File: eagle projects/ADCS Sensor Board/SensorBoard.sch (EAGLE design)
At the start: 85 parts, among them J5 HDR_10_EZFET_DEBUGGER, J6 MTI-1_8428-11B1-RK-TP, Q1 BC850SMD, Q2 IRF7507TRPBF, U1 MSP430F5529IPN, U2 LMV321, U3 ADS7841E_2K5, U4 LMV321, U5 LM20BIM7X_NOPB, U6 LMV321, Y1 32.768kHz, Y2 CSTCR4M00G15L99

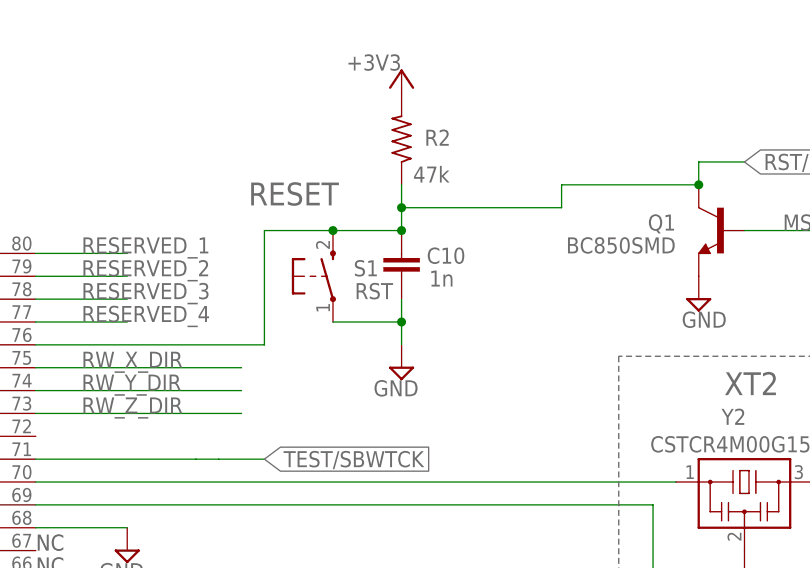
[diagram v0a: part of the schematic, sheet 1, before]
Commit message: Added copper pours to top and bottom. Fixed silksreens, smoothed traces
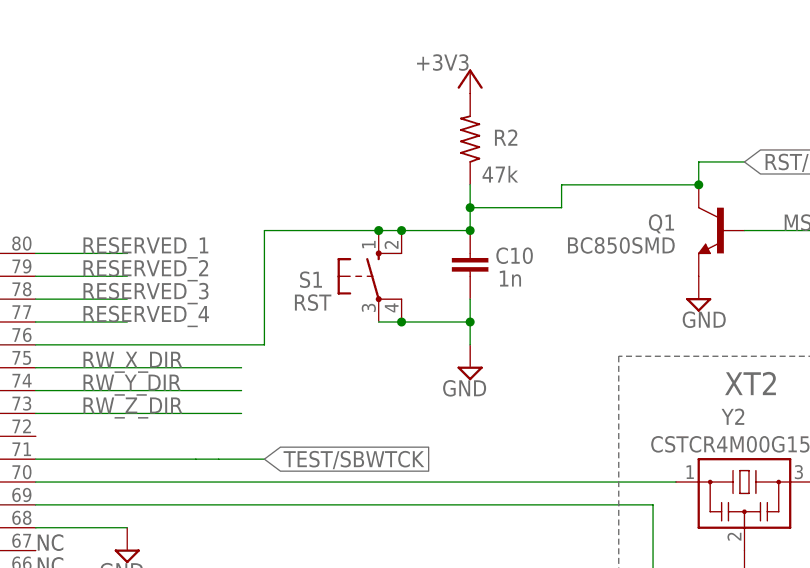
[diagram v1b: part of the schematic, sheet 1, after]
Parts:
- removed SJ1: (no value), jumper:SJ
- added R100: 0R, rcl:R-US_R0603
- JP1: device jumper:JP1Q -> my_library:JP1Q_
- JP2, JP3: device pinhead:PINHD-2X8 -> my_library:PINHD-2X8
- JP4: device pinhead:PINHD-2X6 -> my_library:PINHD-2X6
- JP7: device pinhead:PINHD-1X7 -> my_library:PINHD-1X7
- S1: device electricalmeter:PB -> my_library:10-XX
- TP6: value TPPAD1-13 -> TPB1,27; device testpad:TPPAD1-13 -> testpad:TPB1,27
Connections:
- net GND: now also S1.P1
- net N$35: now also R100.1; no longer SJ1.1
- net N$37: now also R100.2; no longer SJ1.2
- net RST/SBWTDIO: now also S1.S1
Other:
- note removed: "RESET"
- moved on the sheet: C10, R2

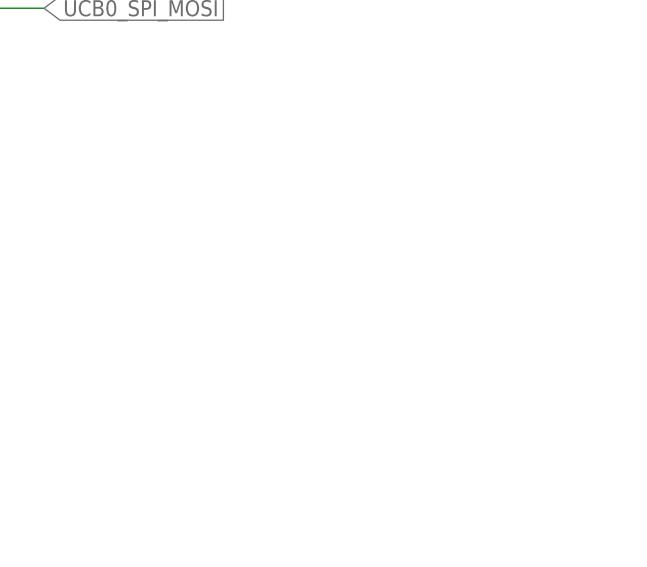
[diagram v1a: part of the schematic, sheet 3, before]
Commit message: Added spi bus test headers
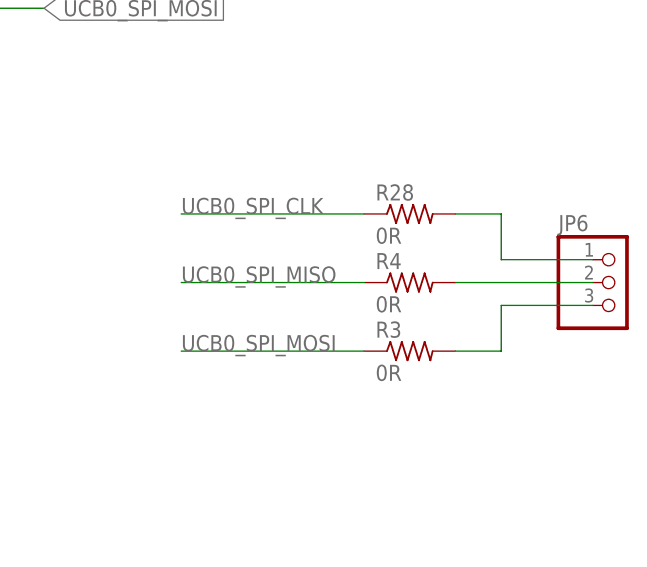
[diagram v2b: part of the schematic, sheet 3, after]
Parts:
- added JP6: (no value), my_library:PINHD-1X3
- added R28, R3, R4: 0R, rcl:R-US_R0805
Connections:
- new net N$1: JP6.1, R28.2
- new net N$2: JP6.2, R4.2
- new net N$3: JP6.3, R3.2
- net UCB0_SPI_CLK: now also R28.1
- net UCB0_SPI_MISO: now also R4.1
- net UCB0_SPI_MOSI: now also R3.1
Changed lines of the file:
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@@
 <schematic_group name="POWER_CONNECTOR"/>
 <schematic_group name="PAYLOAD_CAMERAS"/>
+<schematic_group name="SPI_BUS_TEST"/>
 </groups>
 <parts>
@@
 <part name="SUPPLY31" library="supply2" library_urn="urn:adsk.eagle:library:372" deviceset="GND" device=""/>
 <part name="SUPPLY32" library="supply2" library_urn="urn:adsk.eagle:library:372" deviceset="GND" device=""/>
-<part name="U1" library="my_library" library_urn="urn:adsk.eagle:library:22876504" deviceset="MSP430F5529IPN" device="" package3d_urn="urn:adsk.eagle:package:22927473/4"/>
+<part name="U1" library="my_library" library_urn="urn:adsk.eagle:library:22876504" deviceset="MSP430F5529IPN" device="" package3d_urn="urn:adsk.eagle:package:22927473/5"/>
 <part name="SUPPLY1" library="supply2" library_urn="urn:adsk.eagle:library:372" deviceset="GND" device=""/>
 <part name="SUPPLY2" library="supply2" library_urn="urn:adsk.eagle:library:372" deviceset="GND" device=""/>
@@
 <part name="+3V3" library="supply1" library_urn="urn:adsk.eagle:library:371" deviceset="+3V3" device=""/>
 <part name="S1" library="my_library" library_urn="urn:adsk.eagle:library:22876504" deviceset="10-XX" device="" package3d_urn="urn:adsk.eagle:package:24526167/2" value="RST"/>
+<part name="JP6" library="my_library" library_urn="urn:adsk.eagle:library:22876504" deviceset="PINHD-1X3" device="" package3d_urn="urn:adsk.eagle:package:24583855/1"/>
+<part name="R3" library="rcl" library_urn="urn:adsk.eagle:library:334" deviceset="R-US_" device="R0805" package3d_urn="urn:adsk.eagle:package:23553/2" value="0R"/>
+<part name="R4" library="rcl" library_urn="urn:adsk.eagle:library:334" deviceset="R-US_" device="R0805" package3d_urn="urn:adsk.eagle:package:23553/2" value="0R"/>
+<part name="R28" library="rcl" library_urn="urn:adsk.eagle:library:334" deviceset="R-US_" device="R0805" package3d_urn="urn:adsk.eagle:package:23553/2" value="0R"/>
 </parts>
 <sheets>
@@
 <attribute name="VALUE" x="88.9" y="63.5" size="1.778" layer="96" rot="R180"/>
 </instance>
+<instance part="JP6" gate="A" x="254" y="99.06" smashed="yes" grouprefs="SPI_BUS_TEST">
+<attribute name="NAME" x="247.65" y="104.775" size="1.778" layer="95"/>
+<attribute name="VALUE" x="247.65" y="91.44" size="1.778" layer="96"/>
+</instance>
+<instance part="R3" gate="G$1" x="231.14" y="91.44" smashed="yes" grouprefs="SPI_BUS_TEST">
+<attribute name="NAME" x="227.33" y="92.9386" size="1.778" layer="95"/>
+<attribute name="VALUE" x="227.33" y="88.138" size="1.778" layer="96"/>
+</instance>
+<instance part="R4" gate="G$1" x="231.14" y="99.06" smashed="yes" grouprefs="SPI_BUS_TEST">
+<attribute name="NAME" x="227.33" y="100.5586" size="1.778" layer="95"/>
+<attribute name="VALUE" x="227.33" y="95.758" size="1.778" layer="96"/>
+</instance>
+<instance part="R28" gate="G$1" x="231.14" y="106.68" smashed="yes" grouprefs="SPI_BUS_TEST">
+<attribute name="NAME" x="227.33" y="108.1786" size="1.778" layer="95"/>
+<attribute name="VALUE" x="227.33" y="103.378" size="1.778" layer="96"/>
+</instance>
 </instances>
 <busses>
@@
 <label x="190.5" y="134.62" size="1.778" layer="95" xref="yes"/>
 </segment>
+<segment>
+<pinref part="R28" gate="G$1" pin="1"/>
+<wire x1="226.06" y1="106.68" x2="205.74" y2="106.68" width="0.1524" layer="91" grouprefs="SPI_BUS_TEST"/>
+<label x="205.74" y="106.68" size="1.778" layer="95" grouprefs="SPI_BUS_TEST"/>
+</segment>
 </net>
 <net name="UCB0_SPI_MOSI" class="0">
@@
 <label x="190.5" y="129.54" size="1.778" layer="95" xref="yes"/>
 </segment>
+<segment>
+<pinref part="R3" gate="G$1" pin="1"/>
+<wire x1="205.74" y1="91.44" x2="226.06" y2="91.44" width="0.1524" layer="91" grouprefs="SPI_BUS_TEST"/>
+<label x="205.74" y="91.44" size="1.778" layer="95" grouprefs="SPI_BUS_TEST"/>
+</segment>
 </net>
 <net name="UCB0_SPI_MISO" class="0">
@@
 <wire x1="160.02" y1="132.08" x2="167.64" y2="132.08" width="0.1524" layer="91"/>
 <label x="167.64" y="132.08" size="1.778" layer="95" xref="yes"/>
+</segment>
+<segment>
+<pinref part="R4" gate="G$1" pin="1"/>
+<wire x1="205.74" y1="99.06" x2="226.06" y2="99.06" width="0.1524" layer="91" grouprefs="SPI_BUS_TEST"/>
+<label x="205.74" y="99.06" size="1.778" layer="95" grouprefs="SPI_BUS_TEST"/>
 </segment>
 </net>
@@
 </segment>
 </net>
+<net name="N$1" class="0">
+<segment>
+<pinref part="R28" gate="G$1" pin="2"/>
+<pinref part="JP6" gate="A" pin="1"/>
+<wire x1="236.22" y1="106.68" x2="241.3" y2="106.68" width="0.1524" layer="91" grouprefs="SPI_BUS_TEST"/>
+<wire x1="241.3" y1="106.68" x2="241.3" y2="101.6" width="0.1524" layer="91" grouprefs="SPI_BUS_TEST"/>
+<wire x1="241.3" y1="101.6" x2="251.46" y2="101.6" width="0.1524" layer="91" grouprefs="SPI_BUS_TEST"/>
+</segment>
+</net>
+<net name="N$2" class="0">
+<segment>
+<pinref part="R4" gate="G$1" pin="2"/>
+<pinref part="JP6" gate="A" pin="2"/>
+<wire x1="236.22" y1="99.06" x2="251.46" y2="99.06" width="0.1524" layer="91" grouprefs="SPI_BUS_TEST"/>
+</segment>
+</net>
+<net name="N$3" class="0">
+<segment>
+<pinref part="R3" gate="G$1" pin="2"/>
+<pinref part="JP6" gate="A" pin="3"/>
+<wire x1="251.46" y1="96.52" x2="241.3" y2="96.52" width="0.1524" layer="91" grouprefs="SPI_BUS_TEST"/>
+<wire x1="241.3" y1="96.52" x2="241.3" y2="91.44" width="0.1524" layer="91" grouprefs="SPI_BUS_TEST"/>
+<wire x1="241.3" y1="91.44" x2="236.22" y2="91.44" width="0.1524" layer="91" grouprefs="SPI_BUS_TEST"/>
+</segment>
+</net>

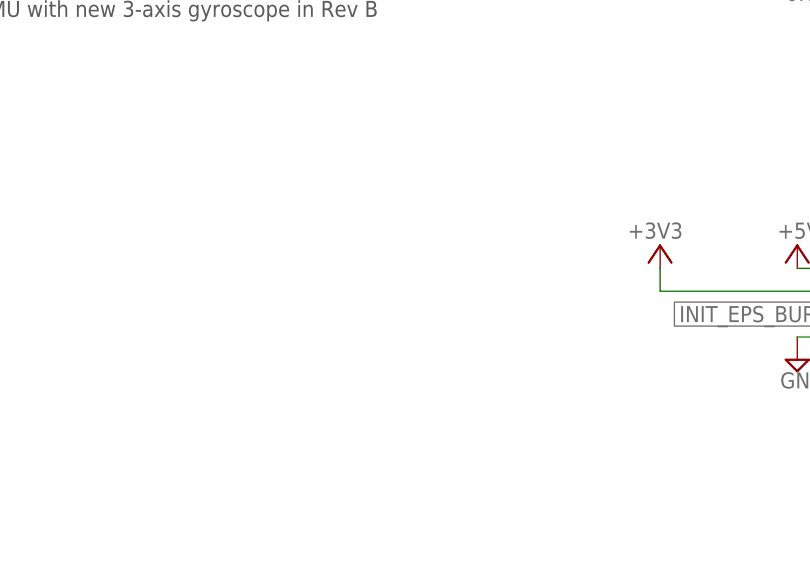
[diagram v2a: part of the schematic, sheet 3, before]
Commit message: added indicator LEDs, drill legend, and adjusted board thickness
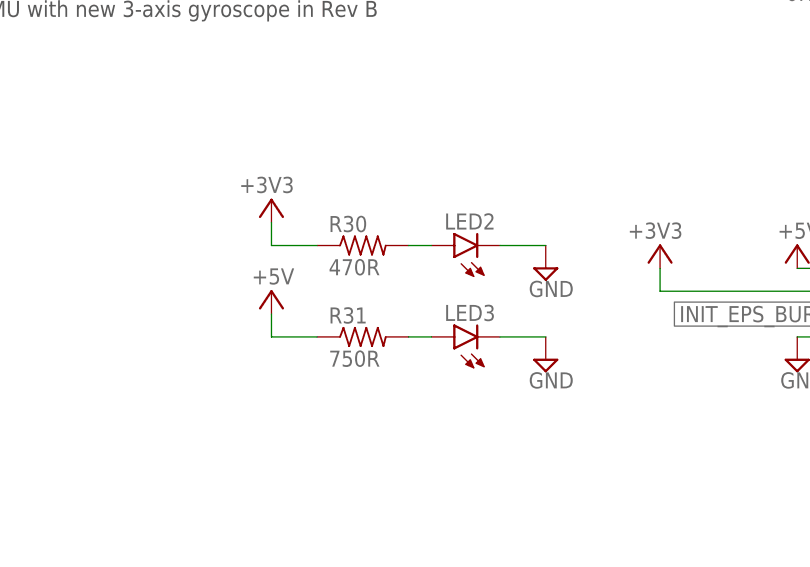
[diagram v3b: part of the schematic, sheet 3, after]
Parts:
- added LED1, LED2, LED3: (no value), led:LEDCHIP-LED0603
- added R29, R30: 470R, rcl:R-US_R0603
- added R31: 750R, rcl:R-US_R0603
- R100: device rcl:R-US_R0603 -> rcl:R-US_R0805
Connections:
- new net N$4: LED1.A, R29.2
- new net N$5: LED2.A, R30.2
- new net N$6: LED3.A, R31.2
- net +3V3: now also R30.1
- net +5V: now also R31.1
- net GND: now also LED1.C, LED2.C, LED3.C
- net MSP430_ACTIVE: now also R29.1
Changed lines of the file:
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@@
 <part name="MH3" library="my_library" library_urn="urn:adsk.eagle:library:22876504" deviceset="MTGP700H400" device="" package3d_urn="urn:adsk.eagle:package:23248012/2"/>
 <part name="MH4" library="my_library" library_urn="urn:adsk.eagle:library:22876504" deviceset="MTGP700H400" device="" package3d_urn="urn:adsk.eagle:package:23248012/2"/>
-<part name="R100" library="rcl" library_urn="urn:adsk.eagle:library:334" deviceset="R-US_" device="R0603" package3d_urn="urn:adsk.eagle:package:23555/3" value="0R"/>
+<part name="R100" library="rcl" library_urn="urn:adsk.eagle:library:334" deviceset="R-US_" device="R0805" package3d_urn="urn:adsk.eagle:package:23553/2" value="0R"/>
 <part name="C20" library="rcl" library_urn="urn:adsk.eagle:library:334" deviceset="C-EU" device="C0805" package3d_urn="urn:adsk.eagle:package:23617/2" value="1n"/>
 <part name="C19" library="rcl" library_urn="urn:adsk.eagle:library:334" deviceset="C-EU" device="C0603" package3d_urn="urn:adsk.eagle:package:23616/2" value="0.1u"/>
@@
 <part name="R4" library="rcl" library_urn="urn:adsk.eagle:library:334" deviceset="R-US_" device="R0805" package3d_urn="urn:adsk.eagle:package:23553/2" value="0R"/>
 <part name="R28" library="rcl" library_urn="urn:adsk.eagle:library:334" deviceset="R-US_" device="R0805" package3d_urn="urn:adsk.eagle:package:23553/2" value="0R"/>
+<part name="SUPPLY13" library="supply2" library_urn="urn:adsk.eagle:library:372" deviceset="GND" device=""/>
+<part name="R29" library="rcl" library_urn="urn:adsk.eagle:library:334" deviceset="R-US_" device="R0603" package3d_urn="urn:adsk.eagle:package:23555/3" value="470R"/>
+<part name="LED1" library="led" library_urn="urn:adsk.eagle:library:259" deviceset="LED" device="CHIP-LED0603" package3d_urn="urn:adsk.eagle:package:15819/3"/>
+<part name="LED2" library="led" library_urn="urn:adsk.eagle:library:259" deviceset="LED" device="CHIP-LED0603" package3d_urn="urn:adsk.eagle:package:15819/3"/>
+<part name="LED3" library="led" library_urn="urn:adsk.eagle:library:259" deviceset="LED" device="CHIP-LED0603" package3d_urn="urn:adsk.eagle:package:15819/3"/>
+<part name="R30" library="rcl" library_urn="urn:adsk.eagle:library:334" deviceset="R-US_" device="R0603" package3d_urn="urn:adsk.eagle:package:23555/3" value="470R"/>
+<part name="R31" library="rcl" library_urn="urn:adsk.eagle:library:334" deviceset="R-US_" device="R0603" package3d_urn="urn:adsk.eagle:package:23555/3" value="750R"/>
+<part name="SUPPLY19" library="supply2" library_urn="urn:adsk.eagle:library:372" deviceset="GND" device=""/>
+<part name="SUPPLY25" library="supply2" library_urn="urn:adsk.eagle:library:372" deviceset="GND" device=""/>
+<part name="+3V4" library="supply1" library_urn="urn:adsk.eagle:library:371" deviceset="+3V3" device=""/>
+<part name="P+2" library="supply1" library_urn="urn:adsk.eagle:library:371" deviceset="+5V" device=""/>
 </parts>
 <sheets>
@@
 <attribute name="VALUE" x="201.295" y="166.37" size="1.778" layer="96"/>
 </instance>
+<instance part="SUPPLY13" gate="GND" x="266.7" y="40.64" smashed="yes">
+<attribute name="VALUE" x="264.795" y="37.465" size="1.778" layer="96"/>
+</instance>
+<instance part="R29" gate="G$1" x="246.38" y="43.18" smashed="yes">
+<attribute name="NAME" x="242.57" y="44.6786" size="1.778" layer="95"/>
+<attribute name="VALUE" x="242.57" y="39.878" size="1.778" layer="96"/>
+</instance>
+<instance part="LED1" gate="G$1" x="256.54" y="43.18" smashed="yes" rot="R90">
+<attribute name="NAME" x="261.112" y="46.736" size="1.778" layer="95" rot="R180"/>
+<attribute name="VALUE" x="261.112" y="48.895" size="1.778" layer="96" rot="R180"/>
+</instance>
 </instances>
 <busses>
@@
 <wire x1="172.72" y1="134.62" x2="210.82" y2="134.62" width="0.1524" layer="91"/>
 <pinref part="SUPPLY11" gate="GND" pin="GND"/>
+</segment>
+<segment>
+<pinref part="LED1" gate="G$1" pin="C"/>
+<pinref part="SUPPLY13" gate="GND" pin="GND"/>
+<wire x1="261.62" y1="43.18" x2="266.7" y2="43.18" width="0.1524" layer="91"/>
 </segment>
 </net>
@@
 <wire x1="213.36" y1="43.18" x2="241.3" y2="43.18" width="0.1524" layer="91"/>
 <label x="220.98" y="43.18" size="1.778" layer="95"/>
+<pinref part="R29" gate="G$1" pin="1"/>
 </segment>
 <segment>
@@
 <pinref part="JP2" gate="A" pin="13"/>
 <label x="22.86" y="40.64" size="1.778" layer="95" grouprefs="ACTUATOR_BOARD_CONNECTORS"/>
+</segment>
+</net>
+<net name="N$4" class="0">
+<segment>
+<pinref part="LED1" gate="G$1" pin="A"/>
+<pinref part="R29" gate="G$1" pin="2"/>
+<wire x1="254" y1="43.18" x2="251.46" y2="43.18" width="0.1524" layer="91"/>
 </segment>
 </net>
@@
 <attribute name="VALUE" x="227.33" y="103.378" size="1.778" layer="96"/>
 </instance>
+<instance part="LED2" gate="G$1" x="190.5" y="60.96" smashed="yes" rot="R90">
+<attribute name="NAME" x="195.072" y="64.516" size="1.778" layer="95" rot="R180"/>
+<attribute name="VALUE" x="195.072" y="66.675" size="1.778" layer="96" rot="R180"/>
+</instance>
+<instance part="LED3" gate="G$1" x="190.5" y="50.8" smashed="yes" rot="R90">
+<attribute name="NAME" x="195.072" y="54.356" size="1.778" layer="95" rot="R180"/>
+<attribute name="VALUE" x="195.072" y="56.515" size="1.778" layer="96" rot="R180"/>
+</instance>
+<instance part="R30" gate="G$1" x="180.34" y="60.96" smashed="yes">
+<attribute name="NAME" x="176.53" y="62.4586" size="1.778" layer="95"/>
+<attribute name="VALUE" x="176.53" y="57.658" size="1.778" layer="96"/>
+</instance>
+<instance part="R31" gate="G$1" x="180.34" y="50.8" smashed="yes">
+<attribute name="NAME" x="176.53" y="52.2986" size="1.778" layer="95"/>
+<attribute name="VALUE" x="176.53" y="47.498" size="1.778" layer="96"/>
+</instance>
+<instance part="SUPPLY19" gate="GND" x="200.66" y="48.26" smashed="yes">
+<attribute name="VALUE" x="198.755" y="45.085" size="1.778" layer="96"/>
+</instance>
+<instance part="SUPPLY25" gate="GND" x="200.66" y="58.42" smashed="yes">
+<attribute name="VALUE" x="198.755" y="55.245" size="1.778" layer="96"/>
+</instance>
+<instance part="+3V4" gate="G$1" x="170.18" y="66.04" smashed="yes">
+<attribute name="VALUE" x="172.72" y="68.58" size="1.778" layer="96" rot="R180"/>
+</instance>
+<instance part="P+2" gate="1" x="170.18" y="55.88" smashed="yes">
+<attribute name="VALUE" x="172.72" y="58.42" size="1.778" layer="96" rot="R180"/>
+</instance>
 </instances>
 <busses>
@@
 <pinref part="+3V3" gate="G$1" pin="+3V3"/>
 </segment>
+<segment>
+<pinref part="+3V4" gate="G$1" pin="+3V3"/>
+<wire x1="170.18" y1="63.5" x2="170.18" y2="60.96" width="0.1524" layer="91"/>
+<pinref part="R30" gate="G$1" pin="1"/>
+<wire x1="170.18" y1="60.96" x2="175.26" y2="60.96" width="0.1524" layer="91"/>
+</segment>
 </net>
 <net name="GND" class="0">
@@
 <wire x1="101.6" y1="66.04" x2="101.6" y2="60.96" width="0.1524" layer="91" grouprefs="EZFET_DEBUGGER_HEADER"/>
 <pinref part="SUPPLY12" gate="GND" pin="GND"/>
+</segment>
+<segment>
+<pinref part="SUPPLY25" gate="GND" pin="GND"/>
+<pinref part="LED2" gate="G$1" pin="C"/>
+<wire x1="200.66" y1="60.96" x2="195.58" y2="60.96" width="0.1524" layer="91"/>
+</segment>
+<segment>
+<pinref part="LED3" gate="G$1" pin="C"/>
+<pinref part="SUPPLY19" gate="GND" pin="GND"/>
+<wire x1="195.58" y1="50.8" x2="200.66" y2="50.8" width="0.1524" layer="91"/>
 </segment>
 </net>
@@
 <wire x1="228.6" y1="58.42" x2="246.38" y2="58.42" width="0.1524" layer="91" grouprefs="POWER_CONNECTOR"/>
 </segment>
+<segment>
+<pinref part="P+2" gate="1" pin="+5V"/>
+<wire x1="170.18" y1="53.34" x2="170.18" y2="50.8" width="0.1524" layer="91"/>
+<pinref part="R31" gate="G$1" pin="1"/>
+<wire x1="170.18" y1="50.8" x2="175.26" y2="50.8" width="0.1524" layer="91"/>
+</segment>
 </net>
 <net name="TEST/SBWTCK" class="0">
@@
 </segment>
 </net>
+<net name="N$5" class="0">
+<segment>
+<pinref part="R30" gate="G$1" pin="2"/>
+<pinref part="LED2" gate="G$1" pin="A"/>
+<wire x1="185.42" y1="60.96" x2="187.96" y2="60.96" width="0.1524" layer="91"/>
+</segment>
+</net>
+<net name="N$6" class="0">
+<segment>
+<pinref part="R31" gate="G$1" pin="2"/>
+<pinref part="LED3" gate="G$1" pin="A"/>
+<wire x1="185.42" y1="50.8" x2="187.96" y2="50.8" width="0.1524" layer="91"/>
+</segment>
+</net>

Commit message: Updated traces/ vias to meet manufacturer DRC
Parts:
- C2: device rcl:CPOL-EUA/3216-18R -> my_library:POLARIZED_CAP
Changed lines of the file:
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@@
 <layer number="144" name="DrillLegend" color="7" fill="1" visible="yes" active="yes"/>
 <layer number="145" name="DrillLegend_01-16" color="2" fill="9" visible="yes" active="yes"/>
+<layer number="146" name="DrillLegend_01-20" color="3" fill="9" visible="yes" active="yes"/>
 <layer number="150" name="Notes" color="7" fill="1" visible="yes" active="yes"/>
 <layer number="151" name="_tDocu" color="7" fill="1" visible="yes" active="yes"/>
@@
 <part name="C4" library="rcl" library_urn="urn:adsk.eagle:library:334" deviceset="C-EU" device="C0402" package3d_urn="urn:adsk.eagle:package:23626/2" value="12p"/>
 <part name="C1" library="rcl" library_urn="urn:adsk.eagle:library:334" deviceset="C-EU" device="C0402" package3d_urn="urn:adsk.eagle:package:23626/2" value="100n"/>
-<part name="C2" library="rcl" library_urn="urn:adsk.eagle:library:334" deviceset="CPOL-EU" device="A/3216-18R" package3d_urn="urn:adsk.eagle:package:23410/2" value="10u"/>
+<part name="C2" library="my_library" library_urn="urn:adsk.eagle:library:22876504" deviceset="POLARIZED_CAP" device="" package3d_urn="urn:adsk.eagle:package:24600667/1" value="10u"/>
 <part name="R5" library="rcl" library_urn="urn:adsk.eagle:library:334" deviceset="R-US_" device="R0402" package3d_urn="urn:adsk.eagle:package:23547/3" value="1M"/>
 <part name="Y2" library="my_library" library_urn="urn:adsk.eagle:library:22876504" deviceset="CSTCR4M00G15L99" device="" package3d_urn="urn:adsk.eagle:package:22927472/2" technology="6M00G53Z" value="CSTCR4M00G15L99"/>
